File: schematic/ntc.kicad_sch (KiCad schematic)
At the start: 2 parts

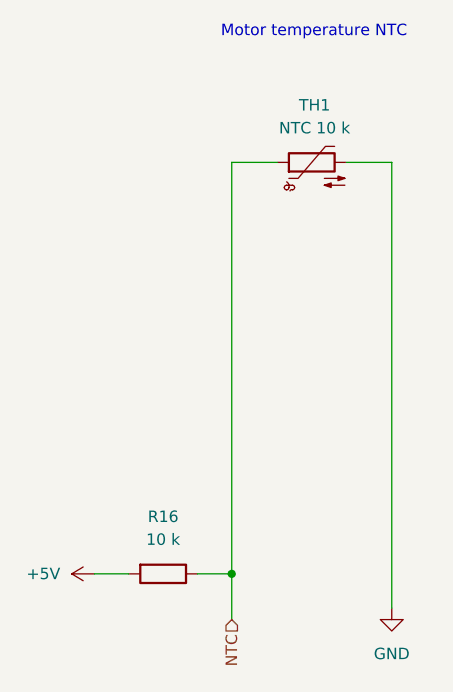
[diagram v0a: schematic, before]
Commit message: schematic: Add 2nd shutoff biasing
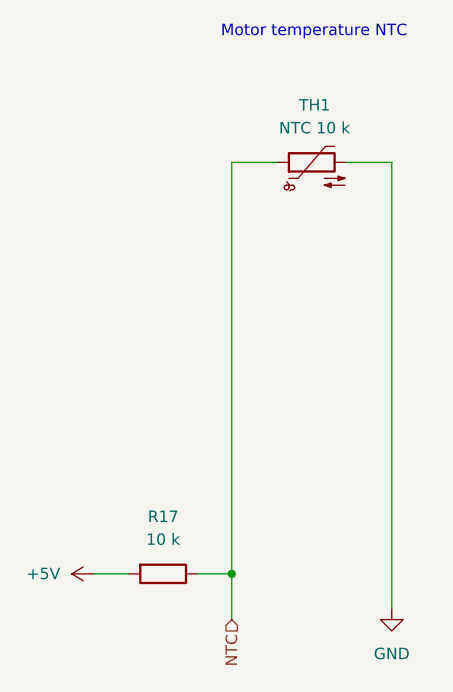
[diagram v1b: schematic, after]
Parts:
- renumbered R16 to R17
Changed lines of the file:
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@@
 		(dnp no)
 		(fields_autoplaced yes)
-		(property "Reference" "#PWR017"
+		(property "Reference" "#PWR018"
 			(at 127 125.73 0)
 			(effects
@@
 			(project "phaseanglecontrol"
 				(path "/167e0419-9f88-4ea4-ae96-d03af9cd26b8/49583429-ecd7-49b9-b636-d7a0d7ebccf5"
-					(reference "#PWR017")
+					(reference "#PWR018")
 					(unit 1)
 				)
@@
 		(dnp no)
 		(fields_autoplaced yes)
-		(property "Reference" "#PWR018"
+		(property "Reference" "#PWR019"
 			(at 156.21 135.89 0)
 			(effects
@@
 			(project "phaseanglecontrol"
 				(path "/167e0419-9f88-4ea4-ae96-d03af9cd26b8/49583429-ecd7-49b9-b636-d7a0d7ebccf5"
-					(reference "#PWR018")
+					(reference "#PWR019")
 					(unit 1)
 				)
@@
 		(dnp no)
 		(fields_autoplaced yes)
-		(property "Reference" "R16"
+		(property "Reference" "R17"
 			(at 130.81 119.38 90)
 			(effects
@@
 			(project "phaseanglecontrol"
 				(path "/167e0419-9f88-4ea4-ae96-d03af9cd26b8/49583429-ecd7-49b9-b636-d7a0d7ebccf5"
-					(reference "R16")
-					(unit 1)
-				)
+					(reference "R17")
+					(unit 1)
+				)
